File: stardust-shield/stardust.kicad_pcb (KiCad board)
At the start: 2 copper layers, 14 parts, among them J1 BEXUS 28V, J2 Pololu J8557, J3 Pololu J9251, J4 DS3231M, U1 MCP1416, U3 MCP1416, U5 DS18B20, U6 DS18B20, U8 DHT22, U9 SSCDRNN015PASA5

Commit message: finish preplacement
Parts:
- removed XA**: Arduino_Mega2560_Shield, Arduino:Arduino_Mega2560_Shield
- moved J1 472.3 mm to (50.8, 56.5), turned to 90 degrees
- moved J2 468.0 mm to (74.9, 36.8)
- moved U5 468.0 mm to (188.0, 75.6)
- moved U6 468.0 mm to (188.0, 104.4)
- moved U8 468.0 mm to (188.0, 91.2)
- moved U9 468.0 mm to (173.4, 87.6)
- moved DSUB-1 468.0 mm to (193.7, 52.1)
- moved DSUB-2 468.0 mm to (193.7, 134.4)
- moved XA1 466.7 mm to (45.7, 145.4)
- moved J3 465.5 mm to (74.9, 66.0)
- moved U1 465.5 mm to (130.6, 42.8)
- moved U3 465.5 mm to (130.5, 35.5)
- moved J4 464.7 mm to (130.8, 76.2)
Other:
- board outline added: 154.3 x 134 mm

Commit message: main pcb
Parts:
- removed U3: MCP1416, Package_TO_SOT_SMD:SOT-23-5
- added REF**: MountingHole_3.2mm_M3_DIN965_Pad, MountingHole:MountingHole_3.2mm_M3_DIN965_Pad, F.Cu at (51.4, 151.8)
- added REF**: MountingHole_3.2mm_M3_DIN965_Pad, MountingHole:MountingHole_3.2mm_M3_DIN965_Pad, F.Cu at (194.3, 151.8)
- added REF**: MountingHole_3.2mm_M3_DIN965_Pad, MountingHole:MountingHole_3.2mm_M3_DIN965_Pad, F.Cu at (51.4, 24.1)
- added REF**: MountingHole_3.2mm_M3_DIN965_Pad, MountingHole:MountingHole_3.2mm_M3_DIN965_Pad, F.Cu at (194.3, 24.1)
- added U2: IRFL210, Package_TO_SOT_SMD:SOT-223-3_TabPin2, B.Cu at (130.8, 59.1)
- U1: value MCP1416 -> IRFL210; footprint Package_TO_SOT_SMD:SOT-23-5 -> Package_TO_SOT_SMD:SOT-223-3_TabPin2; moved to B.Cu
- moved J4 19.7 mm to (111.1, 76.2)
- moved U9 9.86 mm to (163.8, 90.2), turned to 90 degrees
- moved U5 3.23 mm to (191.1, 76.2)
- moved U8 3.18 mm to (191.1, 91.4)
- moved U6 3.13 mm to (191.1, 104.1)
- moved U1 2.81 mm to (130.8, 40.0), turned to 270 degrees
- moved DSUB-2 0.81 mm to (193.7, 135.3)
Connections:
- DSUB-1 pad 2: 1Wire -> 1Wire-1
- DSUB-2 pad 4: 1Wire -> 1Wire-2
- DSUB-2 pad 7: SPI-SS-Pressure -> SPI-SS-Pressure-1
- U1 pad 1: Net-(U1-Pad1) -> +12V
- U1 pad 2: +12V -> Pump-GPIO-1
- U1 pad 3: Pump-GPIO-1 -> Pump-1
- U5 pad 2: 1Wire -> 1Wire-3
- U6 pad 2: 1Wire -> 1Wire-3
- U9 pad 1: VCC -> GND
- U9 pad 2: GND -> +5V
- U9 pad 3: GND -> SPI-MISO
- U9 pad 4: SPI-SS-Pressure -> SPI-CLK
- U9 pad 5: SPI-SS-Pressure -> SPI-SS-Pressure-2
- U9 pad 6: SPI -> (no net)
- U9 pad 7: SPI -> (no net)
- U9 pad 8: SPI -> (no net)
- XA1 pad D22: DHT22-1 -> Net-(XA1-PadD22)
- XA1 pad D23: DHT22-2 -> Pump-GPIO-2
- XA1 pad D24: 1Wire -> Net-(XA1-PadD24)
- XA1 pad D25: DHT22-3 -> Pump-GPIO-1
- XA1 pad D26: SPI-SS-Pressure -> Net-(XA1-PadD26)
- XA1 pad D27: Net-(XA1-PadD27) -> SPI-SS-Pressure-2
- XA1 pad D29: Net-(XA1-PadD29) -> DHT22-1
- XA1 pad D31: Net-(XA1-PadD31) -> 1Wire-1
- XA1 pad D33: Net-(XA1-PadD33) -> DHT22-3
- XA1 pad D35: Pump-GPIO-1 -> 1Wire-3
- XA1 pad D37: Pump-GPIO-2 -> 1Wire-2
- XA1 pad D39: Net-(XA1-PadD39) -> DHT22-2
- XA1 pad D41: Net-(XA1-PadD41) -> SPI-SS-Pressure-1
- XA1 pad GND2: Net-(XA1-PadGND2) -> GND
- XA1 pad GND3: Net-(XA1-PadGND3) -> GND
- XA1 pad GND5: Net-(XA1-PadGND5) -> GND
- XA1 pad GND6: Net-(XA1-PadGND6) -> GND
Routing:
- net I2C-SCL: track 0.00 -> 130.8 mm, vias 0 -> 1
- net I2C-SDA: track 0.00 -> 128.2 mm, vias 0 -> 3
- net DHT22-1: track 0.00 -> 108.4 mm
- net 1Wire-1: track 0.00 -> 105.6 mm
- net SPI-CLK: track 0.00 -> 101.5 mm, vias 0 -> 1
- net SPI-MISO: track 0.00 -> 90.4 mm, vias 0 -> 4
- net Pump-GPIO-1: track 0.00 -> 89.7 mm, vias 0 -> 3
- net 1Wire-3: track 0.00 -> 88.5 mm
- net Pump-GPIO-2: track 0.00 -> 78.2 mm, vias 0 -> 3
- net +12V: track 0.00 -> 74.3 mm
- net Pump-2: track 0.00 -> 69.3 mm
- net Pump-1: track 0.00 -> 67.6 mm
- net DHT22-3: track 0.00 -> 67.2 mm, vias 0 -> 1
- net SPI-SS-Pressure-1: track 0.00 -> 63.3 mm, vias 0 -> 1
- net DHT22-2: track 0.00 -> 63.2 mm
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- added copper zone on F.Cu, net +5V
- added copper zone on B.Cu, net GND
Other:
- board size 154.3 x 134 mm -> 154.3 x 139.1 mm

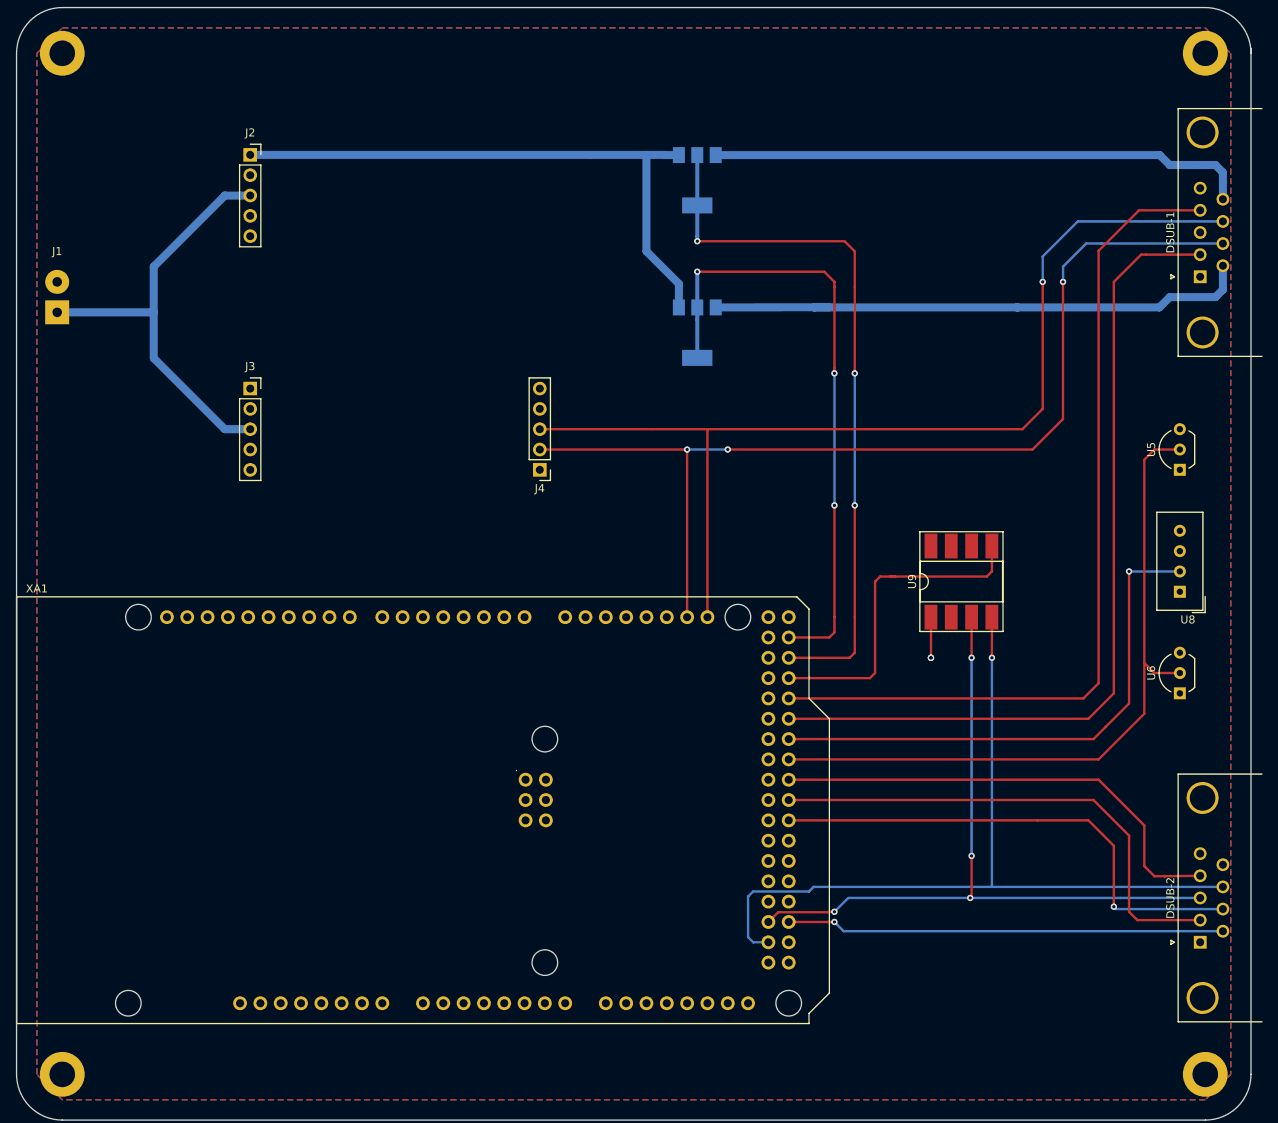
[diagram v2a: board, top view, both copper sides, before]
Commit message: fix border, move mosfet, add  labels
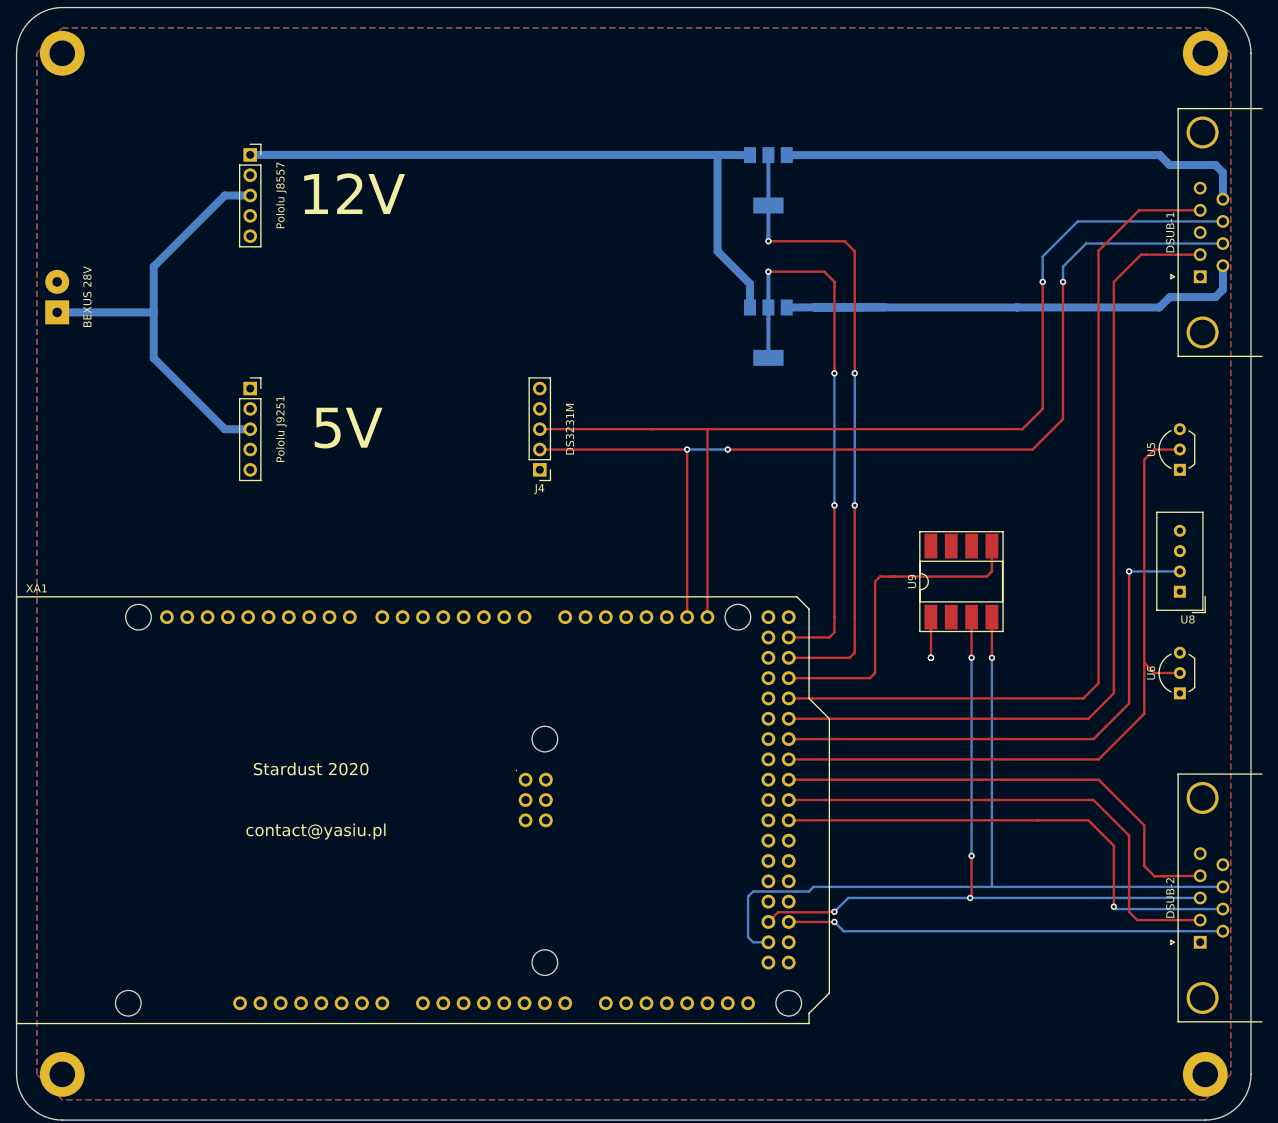
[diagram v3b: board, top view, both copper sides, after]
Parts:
- moved U1 8.89 mm to (139.7, 40.0)
- moved U2 8.89 mm to (139.7, 59.1)
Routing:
- net +12V: track 74.3 -> 83.2 mm
- net Pump-GPIO-2: track 78.2 -> 69.3 mm
- net Pump-GPIO-1: track 89.7 -> 80.8 mm
- net Pump-1: track 67.6 -> 58.8 mm
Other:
- outline, holes or cut-outs redrawn
- board text added: "12V"
- board text added: "5V"
- board text added: "Stardust 2020"
- board text added: "contact@yasiu.pl"

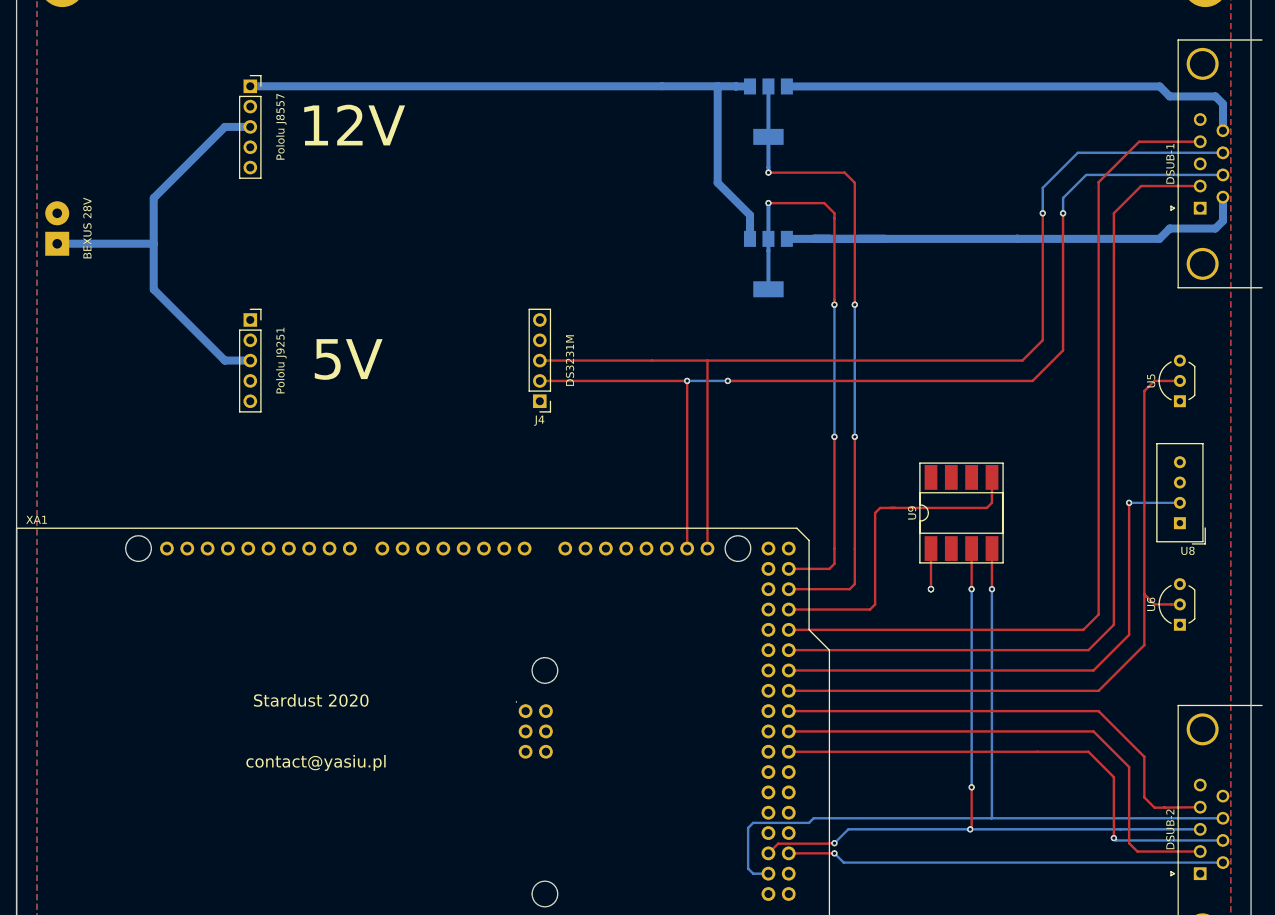
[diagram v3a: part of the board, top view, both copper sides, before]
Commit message: add footprints, clear board
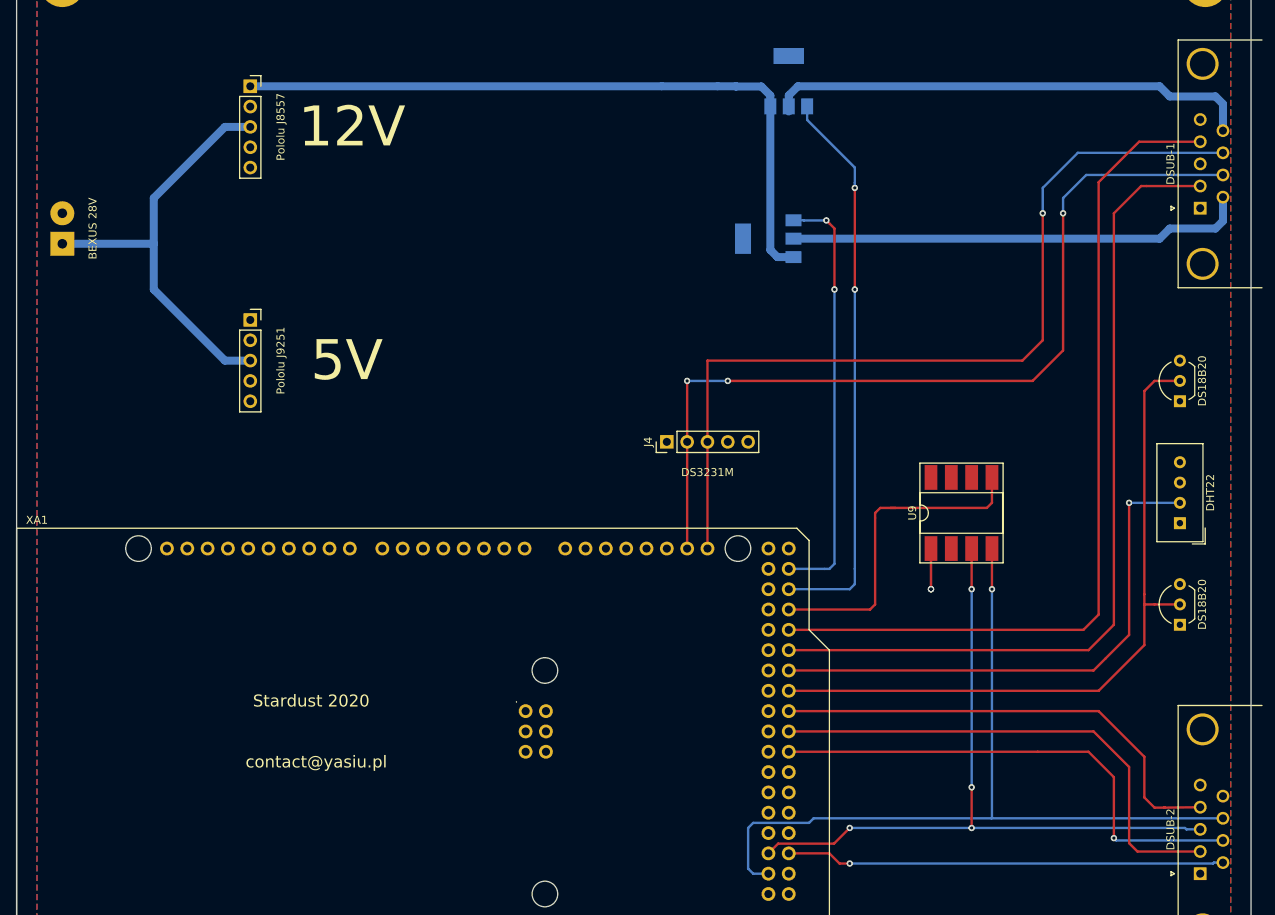
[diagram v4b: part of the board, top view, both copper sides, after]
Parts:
- U1, U2: footprint Package_TO_SOT_SMD:SOT-223-3_TabPin2 -> Package_TO_SOT_SMD:SOT-223
- moved J4 16.7 mm to (127.0, 81.3), turned to 90 degrees
- moved U1 4.58 mm to (142.2, 36.2), turned to 90 degrees
- moved U2 3.18 mm to (139.7, 55.9), turned to 180 degrees
- moved J1 0.64 mm to (51.4, 56.5)
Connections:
- U1 pad 1: +12V -> Pump-GPIO-1
- U1 pad 2: Pump-GPIO-1 -> Pump-1
- U1 pad 3: Pump-1 -> +12V
- U2 pad 1: +12V -> Pump-GPIO-2
- U2 pad 2: Pump-GPIO-2 -> Pump-2
- U2 pad 3: Pump-2 -> +12V
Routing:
- net I2C-SCL: track 130.8 -> 109.8 mm
- net I2C-SDA: track 128.2 -> 109.8 mm
- net Pump-GPIO-2: track 69.3 -> 53.4 mm, vias 3 -> 2
- net Pump-2: track 69.3 -> 57.6 mm
- net Pump-GPIO-1: track 80.8 -> 70.7 mm, vias 3 -> 2
- net +12V: track 83.2 -> 88.7 mm
- net Pump-1: track 58.8 -> 61.0 mm
- net 1Wire-3: track 88.5 -> 88.0 mm

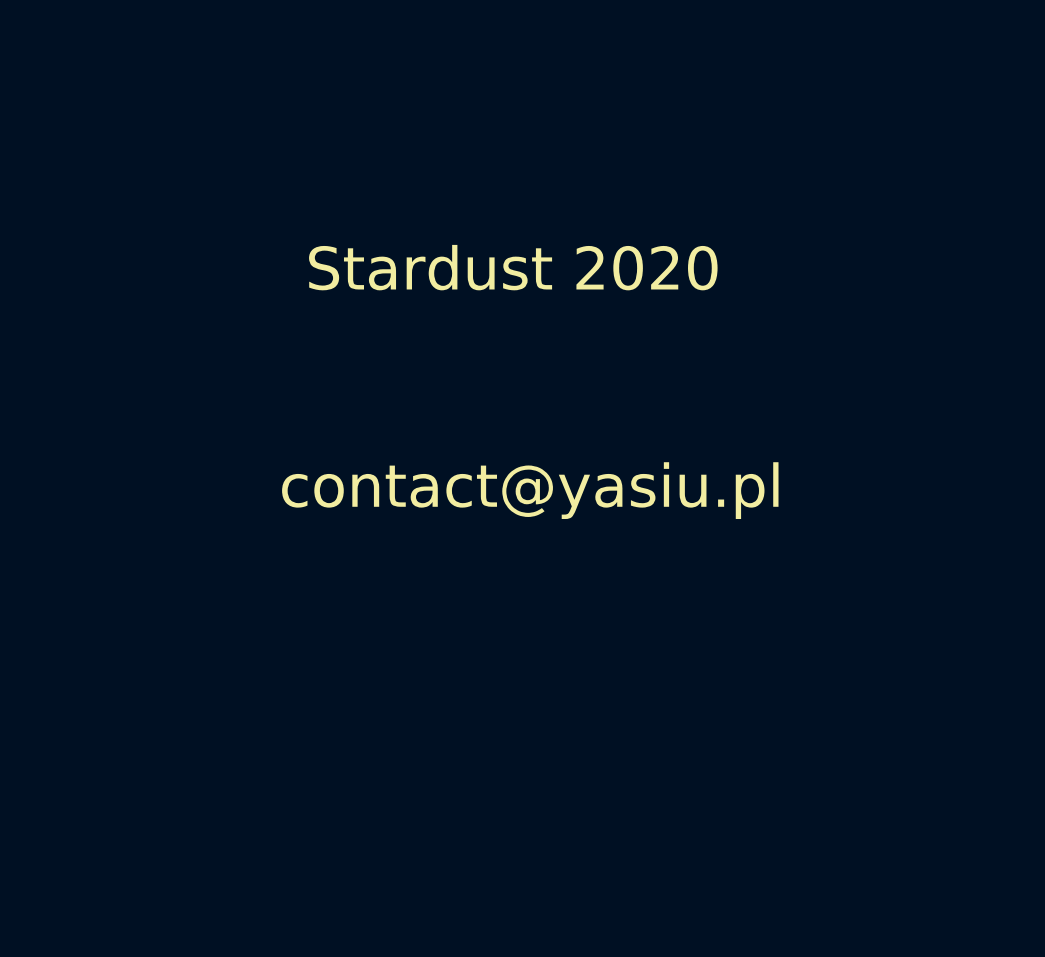
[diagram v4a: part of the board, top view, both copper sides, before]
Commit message: add JLC id placeholder
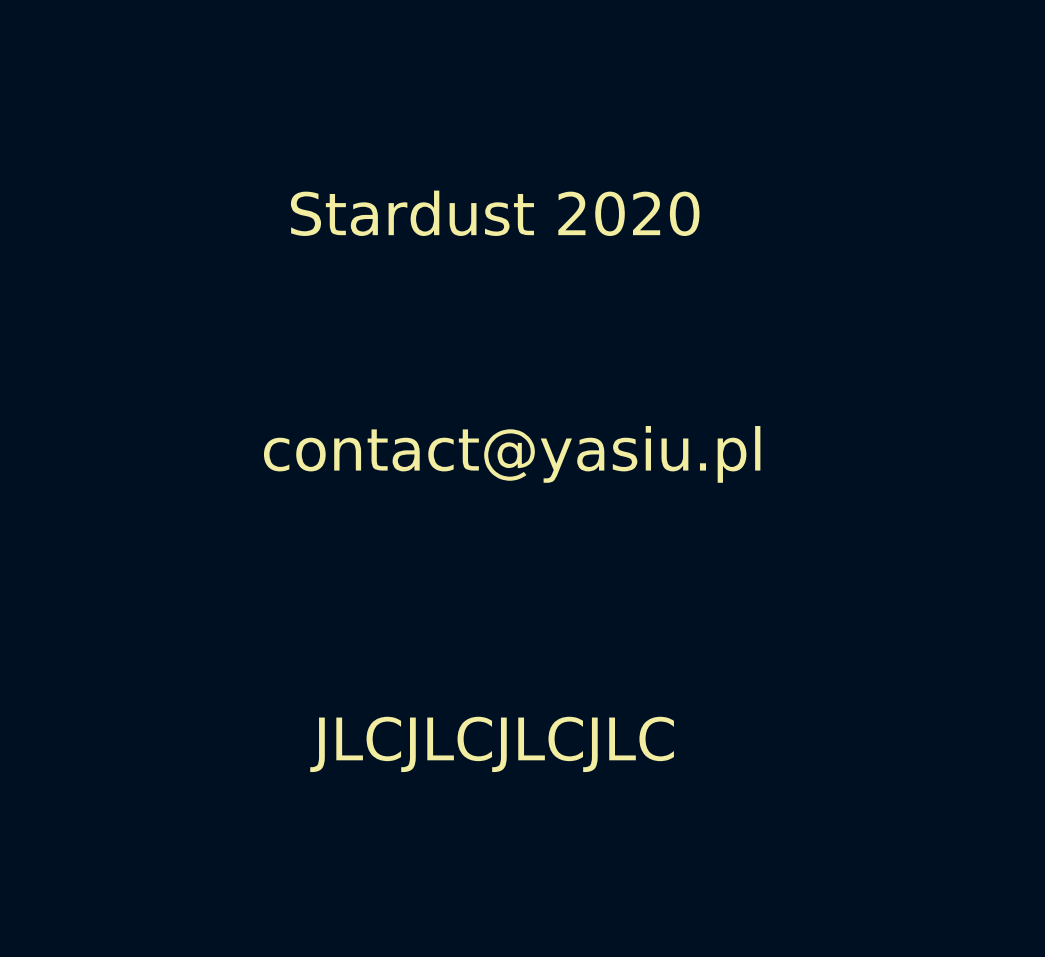
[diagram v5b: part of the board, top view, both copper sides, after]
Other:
- board text added: "JLCJLCJLCJLC"
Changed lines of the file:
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@@
   (general
     (thickness 1.6)
-    (drawings 14)
+    (drawings 15)
     (tracks 185)
     (zones 0)
@@
   )
   (setup
-    (last_trace_width 0.3)
+    (last_trace_width 0.25)
     (user_trace_width 0.3)
     (user_trace_width 0.5)
@@
     )
   )
+  (gr_text JLCJLCJLCJLC (at 81.915 130.175) (layer F.SilkS)
+    (effects (font (size 1.5 1.5) (thickness 0.3)))
+  )
   (dimension 154.305 (width 0.15) (layer Dwgs.User)
     (gr_text "154,305 mm" (at 122.8725 165.13) (layer Dwgs.User)
@@
     (arrow2b (pts (xy 45.72 163.83) (xy 46.846504 163.243579)))
   )
-  (gr_text contact@yasiu.pl (at 83.185 121.285) (layer F.SilkS)
+  (gr_text contact@yasiu.pl (at 82.55 120.015) (layer F.SilkS)
     (effects (font (size 1.5 1.5) (thickness 0.3)))
   )
-  (gr_text "Stardust 2020" (at 82.55 113.665) (layer F.SilkS)
+  (gr_text "Stardust 2020" (at 81.915 111.76) (layer F.SilkS)
     (effects (font (size 1.5 1.5) (thickness 0.3)))
   )
@@
   (segment (start 195.58 38.1) (end 196.515 39.035) (width 1) (layer B.Cu) (net 2))
   (segment (start 189.865 38.1) (end 195.58 38.1) (width 1) (layer B.Cu) (net 2))
+  (segment (start 142.24 37.98) (end 143.39 36.83) (width 1) (layer B.Cu) (net 2))
+  (segment (start 142.24 39.98) (end 142.24 37.98) (width 1) (layer B.Cu) (net 2))
+  (segment (start 188.595 36.83) (end 189.865 38.1) (width 1) (layer B.Cu) (net 2))
+  (segment (start 143.39 36.83) (end 188.595 36.83) (width 1) (layer B.Cu) (net 2))
   (segment (start 173.99 49.53) (end 173.99 52.705) (width 0.3) (layer B.Cu) (net 3))
   (segment (start 196.515 45.145) (end 178.375 45.145) (width 0.3) (layer B.Cu) (net 3))
@@
   (via (at 176.53 52.705) (size 0.8) (drill 0.4) (layers F.Cu B.Cu) (net 4))
   (segment (start 134.62 73.66) (end 129.54 73.66) (width 0.3) (layer B.Cu) (net 4))
-  (segment (start 142.24 37.98) (end 143.39 36.83) (width 1) (layer B.Cu) (net 2))
-  (segment (start 142.24 39.98) (end 142.24 37.98) (width 1) (layer B.Cu) (net 2))
-  (segment (start 188.595 36.83) (end 189.865 38.1) (width 1) (layer B.Cu) (net 2))
-  (segment (start 143.39 36.83) (end 188.595 36.83) (width 1) (layer B.Cu) (net 2))
   (segment (start 196.515 53.675) (end 196.515 50.685) (width 1) (layer B.Cu) (net 5))
   (segment (start 195.58 54.61) (end 196.515 53.675) (width 1) (layer B.Cu) (net 5))
